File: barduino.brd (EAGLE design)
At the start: 54.9 x 47.4 mm, 26 parts, among them Q2 16MHz, X1 MINI-USB-PWR

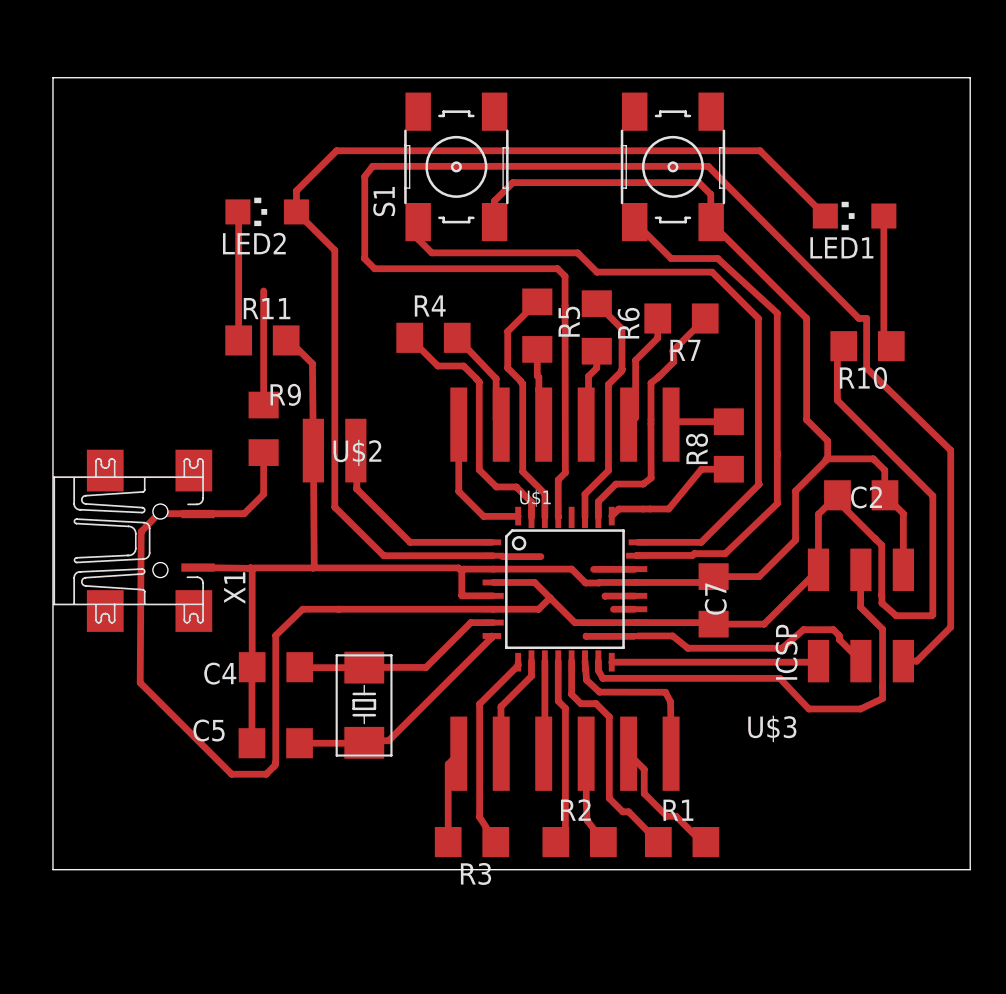
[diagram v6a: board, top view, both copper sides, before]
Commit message: align schematic, add another resistor
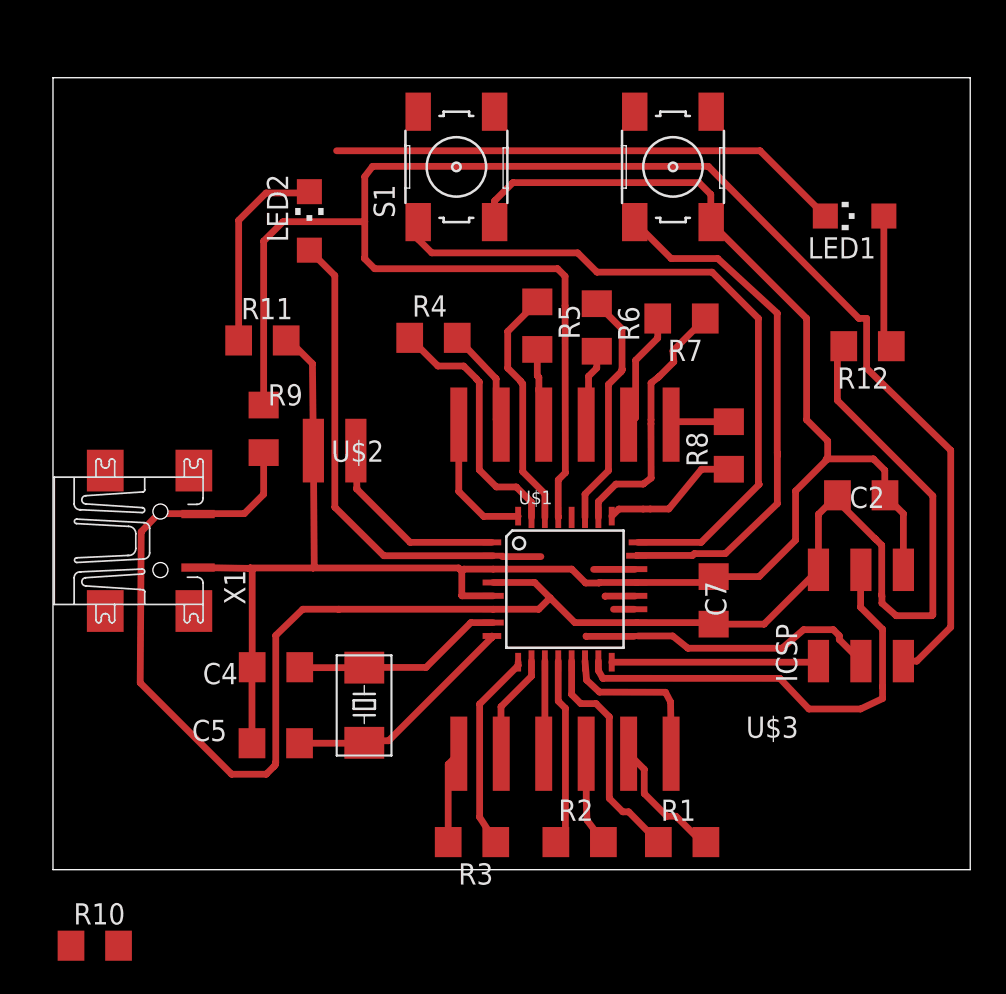
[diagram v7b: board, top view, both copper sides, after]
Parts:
- added R12: (no value), resistor:R1206
- moved R10 58.5 mm to (-17.3, 7.77), turned to 0 degrees
- moved LED2 2.58 mm to (-4.48, 51.1), turned to 0 degrees
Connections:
- net D4: now also R10.1, R10.2
- net N$1: now also R12.1; no longer R10.1
- net VCC: now also R12.2; no longer R10.2
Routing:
- net RESET: track 97.2 -> 106.7 mm
- net D4: track 64.8 -> 57.5 mm
- net N$2: track 7.71 -> 12.1 mm
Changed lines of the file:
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@@
 <element name="R4" library="resistor" package="R1206" value="" x="2.9464" y="44.132503125"/>
 <element name="LED1" library="led" package="CHIPLED_1206" value="AM" x="28.135465625" y="51.417225" rot="R90"/>
-<element name="LED2" library="led" package="CHIPLED_1206" value="PM" x="-7.000246875" y="51.663603125" rot="R90"/>
-<element name="R10" library="resistor" package="R1206" value="" x="28.910275" y="43.63211875" rot="R180"/>
+<element name="LED2" library="led" package="CHIPLED_1206" value="PM" x="-4.475478125" y="51.125125"/>
+<element name="R12" library="resistor" package="R1206" value="" x="28.910275" y="43.63211875" rot="R180"/>
 <element name="R5" library="resistor" package="R1206" value="" x="9.156703125" y="44.861478125" rot="R270"/>
 <element name="R6" library="resistor" package="R1206" value="" x="12.715240625" y="44.7522625" rot="R270"/>
@@
 <element name="X1" library="4-Digit-Clock" package="UX60-MB-5ST-PWR" value="MINI-USB-PWR" x="-13.3858" y="31.991296875"/>
 <element name="R11" library="resistor" package="R1206" value="" x="-7.28471875" y="43.975021875"/>
+<element name="R10" library="resistor" package="R1206" value="" x="-17.312640625" y="7.7724"/>
 </elements>
 <signals>
@@
 <wire x1="-11.110196875" y1="33.6169" x2="-11.1358" y2="33.591296875" width="0.4064" layer="1"/>
 <wire x1="-7.21111875" y1="37.26726875" x2="-7.21111875" y2="34.772540625" width="0.4064" layer="1"/>
-<contactref element="R10" pad="2"/>
+<contactref element="R12" pad="2"/>
 <wire x1="27.107053125" y1="40.388365625" x2="27.107053125" y2="43.250896875" width="0.4064" layer="1"/>
 <wire x1="27.107053125" y1="43.250896875" x2="27.488275" y2="43.63211875" width="0.4064" layer="1"/>
@@
 <wire x1="33.886440625" y1="37.40628125" x2="28.854403125" y2="42.30878125" width="0.4064" layer="1"/>
 <wire x1="28.854403125" y1="42.30878125" x2="28.854403125" y2="45.29581875" width="0.4064" layer="1"/>
-<wire x1="-7.21111875" y1="40.11126875" x2="-7.21111875" y2="46.937753125" width="0.4064" layer="1"/>
 <wire x1="10.817859375" y1="46.05390625" x2="10.817859375" y2="47.818040625" width="0.4064" layer="1"/>
 <wire x1="10.817859375" y1="47.818040625" x2="10.37081875" y2="48.26508125" width="0.4064" layer="1"/>
@@
 <wire x1="19.38781875" y1="54.389021875" x2="-0.695959375" y2="54.389021875" width="0.4064" layer="1"/>
 <wire x1="-0.695959375" y1="54.389021875" x2="-1.16331875" y2="53.77688125" width="0.4064" layer="1"/>
-<wire x1="-1.16331875" y1="53.77688125" x2="-1.16331875" y2="48.908003125" width="0.4064" layer="1"/>
+<wire x1="-1.16331875" y1="51.0794" x2="-1.16331875" y2="53.77688125" width="0.4064" layer="1"/>
+<wire x1="-1.16331875" y1="51.0794" x2="-1.16331875" y2="48.908003125" width="0.4064" layer="1"/>
 <wire x1="-1.16331875" y1="48.908003125" x2="-1.18871875" y2="48.882603125" width="0.4064" layer="1"/>
-<wire x1="-7.21111875" y1="46.937753125" x2="-1.18871875" y2="48.882603125" width="0" layer="19" extent="1-1"/>
+<wire x1="-7.21111875" y1="49.9185625" x2="-6.05028125" y2="51.0794" width="0.4064" layer="1"/>
+<wire x1="-6.05028125" y1="51.0794" x2="-1.16331875" y2="51.0794" width="0.4064" layer="1"/>
+<wire x1="-7.21111875" y1="40.11126875" x2="-7.21111875" y2="49.9185625" width="0.4064" layer="1"/>
 </signal>
 <signal name="PB6">
@@
 <contactref element="LED2" pad="A"/>
 <contactref element="LED1" pad="C"/>
-<wire x1="-5.250246875" y1="51.663603125" x2="-5.250246875" y2="52.920834375" width="0.4064" layer="1"/>
-<wire x1="-5.250246875" y1="52.920834375" x2="-2.84988125" y2="55.3212" width="0.4064" layer="1"/>
 <wire x1="22.481490625" y1="55.3212" x2="26.385465625" y2="51.417225" width="0.4064" layer="1"/>
 <wire x1="-2.84988125" y1="55.3212" x2="22.481490625" y2="55.3212" width="0.4064" layer="1"/>
-<wire x1="-2.95401875" y1="34.000440625" x2="-2.95401875" y2="49.367375" width="0.4064" layer="1"/>
-<wire x1="-2.95401875" y1="49.367375" x2="-5.250246875" y2="51.663603125" width="0.4064" layer="1"/>
+<wire x1="-2.95401875" y1="34.000440625" x2="-2.95401875" y2="47.853665625" width="0.4064" layer="1"/>
+<wire x1="-2.95401875" y1="47.853665625" x2="-4.475478125" y2="49.375125" width="0.4064" layer="1"/>
+<contactref element="R10" pad="1"/>
+<contactref element="R10" pad="2"/>
+<wire x1="-4.475478125" y1="49.375125" x2="-2.84988125" y2="55.3212" width="0" layer="19" extent="1-1"/>
+<wire x1="-15.890640625" y1="7.7724" x2="-0.026478125" y2="31.0983" width="0" layer="19" extent="1-1"/>
+<wire x1="-18.734640625" y1="7.7724" x2="-15.890640625" y2="7.7724" width="0" layer="19" extent="1-1"/>
 </signal>
 <signal name="D5">
@@
 <signal name="N$1" class="1">
 <contactref element="LED1" pad="A"/>
-<contactref element="R10" pad="1"/>
+<contactref element="R12" pad="1"/>
 <wire x1="29.885465625" y1="51.417225" x2="29.885465625" y2="44.078928125" width="0.4064" layer="1"/>
 <wire x1="29.885465625" y1="44.078928125" x2="30.332275" y2="43.63211875" width="0.4064" layer="1"/>
@@
 <contactref element="LED2" pad="C"/>
 <contactref element="R11" pad="1"/>
-<wire x1="-8.70671875" y1="43.975021875" x2="-8.70671875" y2="51.620075" width="0.4064" layer="1"/>
-<wire x1="-8.70671875" y1="51.620075" x2="-8.750246875" y2="51.663603125" width="0.4064" layer="1"/>
+<wire x1="-8.70671875" y1="43.975021875" x2="-8.70671875" y2="51.158540625" width="0.4064" layer="1"/>
+<wire x1="-8.70671875" y1="51.158540625" x2="-7.06881875" y2="52.796440625" width="0.4064" layer="1"/>
+<wire x1="-7.06881875" y1="52.796440625" x2="-4.5541625" y2="52.796440625" width="0.4064" layer="1"/>
+<wire x1="-4.5541625" y1="52.796440625" x2="-4.475478125" y2="52.875125" width="0.4064" layer="1"/>
 </signal>
 </signals>

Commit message: fixed mistake on LEDs net
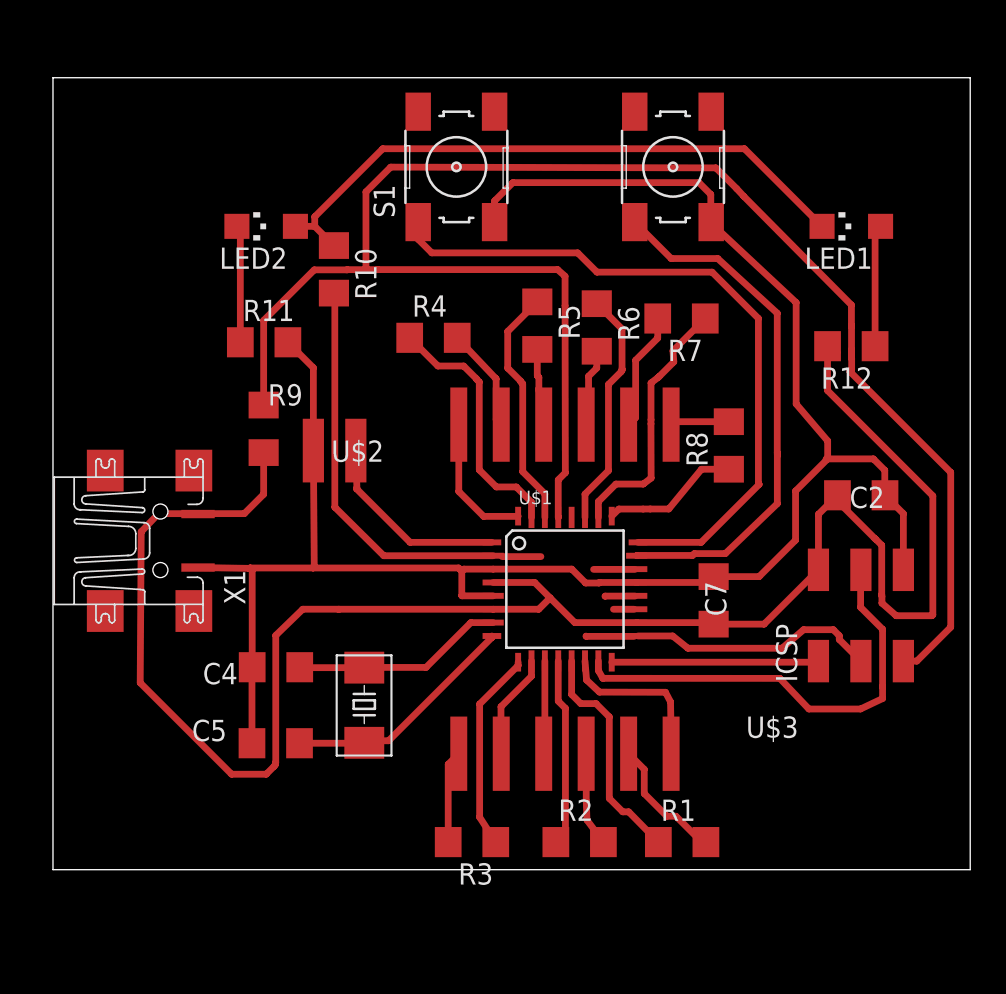
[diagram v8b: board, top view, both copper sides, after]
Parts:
- moved R10 42.9 mm to (-3.01, 48.2), turned to 270 degrees
- moved LED2 2.61 mm to (-7.06, 50.8), turned to 90 degrees
- moved R12 0.97 mm to (27.9, 43.6)
- moved LED1 0.65 mm to (27.9, 50.8)
- moved R11 0.15 mm to (-7.18, 43.9)
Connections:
- new net N$3: LED1.C, LED2.A, R10.1
- net D4: no longer LED1.C, LED2.A, R10.1
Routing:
- net N$3: track 0.00 -> 37.3 mm
- net D4: track 57.5 -> 23.5 mm
- net N$2: track 12.1 -> 7.02 mm
- net RESET: track 106.7 -> 102.3 mm
- net VCC: track 111.6 -> 112.4 mm
